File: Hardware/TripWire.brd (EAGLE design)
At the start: 37.2 x 50.3 mm, 67 parts, among them P1 LSP11, P2 LSP11, P3 LSP11, P4 LSP11, P5 LSP11, P6 LSP11, P7 LSP11, X1 GADGETEER-SOCKET

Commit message: Moved OSHW logo.
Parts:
- moved LOGO1 28.1 mm to (15.6, 32.3)
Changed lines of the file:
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@@
 <layer number="151" name="HeatSink" color="14" fill="1" visible="no" active="no"/>
 <layer number="199" name="Contour" color="7" fill="1" visible="no" active="no"/>
-<layer number="200" name="200bmp" color="7" fill="10" visible="yes" active="yes"/>
-<layer number="201" name="201bmp" color="15" fill="10" visible="yes" active="yes"/>
+<layer number="200" name="200bmp" color="7" fill="10" visible="no" active="yes"/>
+<layer number="201" name="201bmp" color="15" fill="10" visible="no" active="yes"/>
 <layer number="202" name="202bmp" color="7" fill="1" visible="no" active="yes"/>
 <layer number="203" name="203bmp" color="7" fill="1" visible="no" active="yes"/>
@@
 <circle x="33.6346" y="3.6016" radius="3.5355" width="0.4064" layer="20"/>
 <circle x="3.58" y="3.5" radius="3.5355" width="0.4064" layer="20"/>
-<text x="11.30401875" y="7.79131875" size="1.27" layer="21" ratio="12" rot="SR270">TripWire</text>
-<text x="9.830821875" y="5.330059375" size="0.8128" layer="21" ratio="12" rot="SR270">1.2</text>
+<text x="11.81201875" y="9.06131875" size="1.4224" layer="21" ratio="12" rot="SR270">TripWire</text>
+<text x="9.932421875" y="6.320659375" size="1.016" layer="21" ratio="12" rot="SR270">1.2</text>
 <text x="5.4102" y="41.7576" size="1.016" layer="21" ratio="12" rot="SR270">http://ianlee.info</text>
 <text x="-0.6096" y="-3.2512" size="1.778" layer="21">Corner holes are non-plated</text>
@@
 <wire x1="27.0002" y1="10.5918" x2="37.1094" y2="10.5918" width="0.4064" layer="21"/>
 <wire x1="37.1094" y1="10.5918" x2="37.1094" y2="39.8526" width="0.4064" layer="21"/>
-<wire x1="37.1856" y1="30.2768" x2="26.797" y2="30.2768" width="0.4064" layer="21"/>
+<wire x1="37.0586" y1="30.2768" x2="27.051" y2="30.2768" width="0.4064" layer="21"/>
 <wire x1="37.1856" y1="20.193" x2="27.1526" y2="20.193" width="0.4064" layer="21"/>
 <wire x1="20.6756" y1="0.0254" x2="23.41371875" y2="0.0254" width="0.4064" layer="21"/>
@@
 <attribute name="VALUE" x="2.295" y="17.7838" size="0.0254" layer="27" rot="R90"/>
 </element>
-<element name="LOGO1" library="SparkFun-Aesthetics" package="OSHW-LOGO-M" value="OSHW-LOGOM" x="27.0256" y="6.5278" rot="R270"/>
+<element name="LOGO1" library="SparkFun-Aesthetics" package="OSHW-LOGO-M" value="OSHW-LOGOM" x="15.6464" y="32.258" rot="R270"/>
 <element name="R22" library="SparkFun-Resistors" package="0603-RES" value="10" x="17.833340625" y="22.10561875" smashed="yes">
 <attribute name="NAME" x="19.382740625" y="21.80081875" size="0.6096" layer="25" font="vector"/>

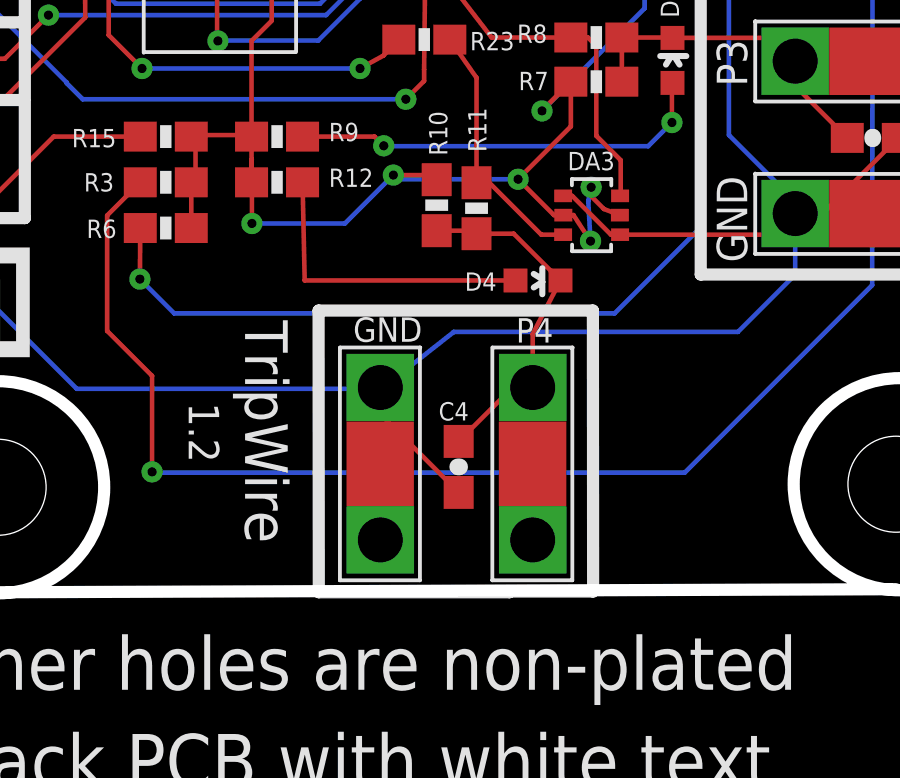
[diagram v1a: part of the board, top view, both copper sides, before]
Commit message: Adjusted font & silk around P4.
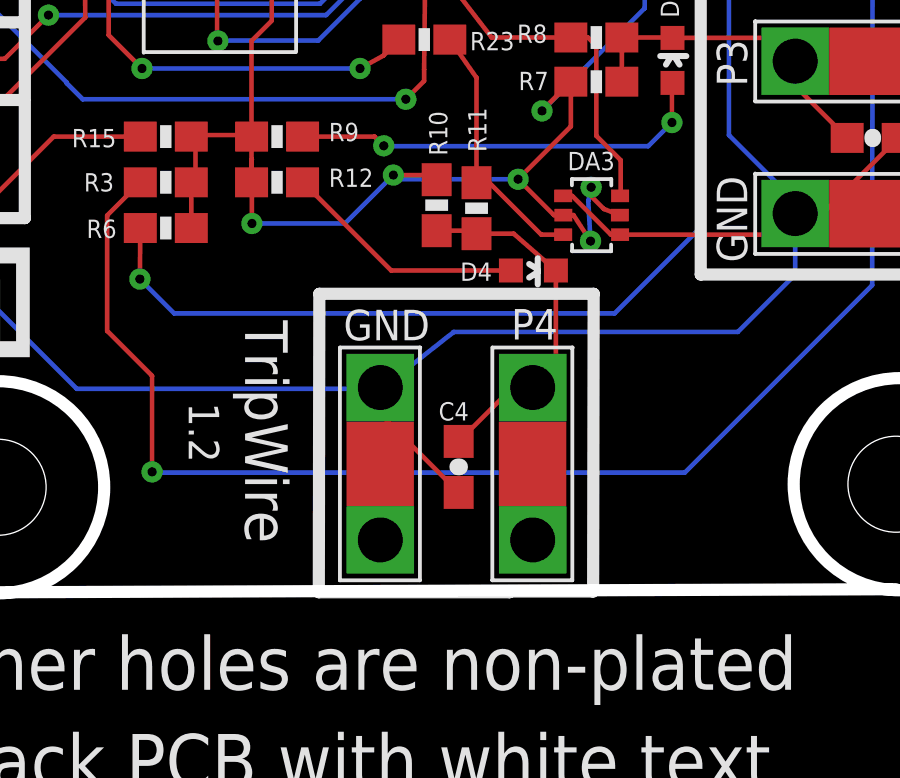
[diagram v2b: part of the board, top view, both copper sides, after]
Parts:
- moved D4 0.36 mm to (21.4, 10.7)
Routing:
- net N$7: track 10.3 -> 8.15 mm
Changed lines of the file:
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@@
 <text x="28.5242" y="27.051" size="1.016" layer="25" rot="R90">P2</text>
 <text x="28.5496" y="16.8656" size="1.016" layer="25" rot="R90">P3</text>
-<text x="22.0853" y="9.136378125" size="0.8128" layer="25" rot="R180">P4</text>
+<text x="22.2377" y="9.441178125" size="1.016" layer="25" rot="R180">P4</text>
 <text x="15.483840625" y="48.73498125" size="1.016" layer="25">P5</text>
 <text x="18.023840625" y="48.68418125" size="1.016" layer="25">P6</text>
@@
 <text x="28.5242" y="31.3436" size="1.016" layer="21" rot="R90">GND</text>
 <text x="28.5496" y="10.9982" size="1.016" layer="21" rot="R90">GND</text>
-<text x="17.7165" y="9.161778125" size="0.8128" layer="21" rot="R180">GND</text>
+<text x="17.9705" y="9.415778125" size="1.016" layer="21" rot="R180">GND</text>
 <text x="14.798040625" y="46.21658125" size="0.6096" layer="21" rot="R90">GND</text>
 <text x="6.1722" y="30.5816" size="1.4224" layer="21" rot="SR270">XY</text>
@@
 <wire x1="37.1856" y1="20.193" x2="27.1526" y2="20.193" width="0.4064" layer="21"/>
 <wire x1="20.6756" y1="0.0254" x2="23.41371875" y2="0.0254" width="0.4064" layer="21"/>
-<wire x1="23.41371875" y1="0.0254" x2="23.4061" y2="9.390378125" width="0.4064" layer="21"/>
-<wire x1="23.4061" y1="9.390378125" x2="14.2621" y2="9.390378125" width="0.4064" layer="21"/>
-<wire x1="14.2621" y1="9.390378125" x2="14.26971875" y2="0" width="0.4064" layer="21"/>
+<wire x1="23.41371875" y1="0.0254" x2="23.4315" y2="9.949178125" width="0.4064" layer="21"/>
+<wire x1="23.4315" y1="9.949178125" x2="14.2875" y2="9.949178125" width="0.4064" layer="21"/>
+<wire x1="14.2875" y1="9.949178125" x2="14.26971875" y2="0" width="0.4064" layer="21"/>
 <wire x1="14.26971875" y1="0" x2="20.6248" y2="0" width="0.4064" layer="21"/>
 <wire x1="20.6248" y1="0" x2="20.6248" y2="0.0254" width="0.4064" layer="21"/>
@@
 <attribute name="VALUE" x="11.7094" y="15.0114" size="0.4064" layer="27" font="vector"/>
 </element>
-<element name="D4" library="SparkFun-LED" package="LED-0603" value="Green 10mA" x="21.574759375" y="10.393678125" smashed="yes" rot="R270">
-<attribute name="PROD_ID" value="DIO-09003" x="44.434759375" y="23.093678125" size="1.778" layer="27" rot="R270" display="off"/>
-<attribute name="NAME" x="19.136359375" y="10.050778125" size="0.6096" layer="25"/>
+<element name="D4" library="SparkFun-LED" package="LED-0603" value="Green 10mA" x="21.422359375" y="10.723878125" smashed="yes" rot="R270">
+<attribute name="PROD_ID" value="DIO-09003" x="44.282359375" y="23.423878125" size="1.778" layer="27" rot="R270" display="off"/>
+<attribute name="NAME" x="18.983959375" y="10.380978125" size="0.6096" layer="25"/>
 </element>
 <element name="R10" library="SparkFun-Resistors" package="0603-RES" value="100K" x="18.1991" y="12.9032" smashed="yes" rot="R270">
@@
 <contactref element="U$7" pad="P$1"/>
 <contactref element="C4" pad="1"/>
-<wire x1="22.324759375" y1="10.393678125" x2="21.3995" y2="8.608759375" width="0.154" layer="1"/>
-<wire x1="21.3995" y1="8.608759375" x2="21.3995" y2="6.824978125" width="0.154" layer="1"/>
 <wire x1="19.527521875" y1="11.9516" x2="19.425921875" y2="12.0532" width="0.154" layer="1"/>
 <wire x1="19.425921875" y1="12.0532" x2="18.1991" y2="12.0532" width="0.154" layer="1"/>
-<wire x1="22.324759375" y1="10.393678125" x2="20.7668375" y2="11.9516" width="0.154" layer="1"/>
+<wire x1="22.172359375" y1="10.723878125" x2="20.7668375" y2="11.9516" width="0.154" layer="1"/>
 <wire x1="20.7668375" y1="11.9516" x2="19.527521875" y2="11.9516" width="0.154" layer="1"/>
 <wire x1="18.93188125" y1="5.029540625" x2="20.709540625" y2="6.8072" width="0.154" layer="1"/>
 <wire x1="20.709540625" y1="6.8072" x2="21.4122" y2="6.8072" width="0.154" layer="1"/>
+<wire x1="21.4122" y1="6.8072" x2="21.3995" y2="6.824978125" width="0" layer="19" extent="1-1"/>
+<wire x1="22.172359375" y1="10.723878125" x2="22.172359375" y2="7.567359375" width="0.154" layer="1"/>
+<wire x1="22.172359375" y1="7.567359375" x2="21.4122" y2="6.8072" width="0.154" layer="1"/>
 <wire x1="21.4122" y1="6.8072" x2="21.3995" y2="6.824978125" width="0" layer="19" extent="1-16"/>
 </signal>
@@
 <contactref element="R12" pad="2"/>
 <contactref element="D4" pad="A"/>
-<wire x1="13.7278" y1="13.6652" x2="13.798921875" y2="10.393678125" width="0.154" layer="1"/>
-<wire x1="13.798921875" y1="10.393678125" x2="20.824759375" y2="10.393678125" width="0.154" layer="1"/>
+<wire x1="20.672359375" y1="10.723878125" x2="16.682721875" y2="10.723878125" width="0.154" layer="1"/>
+<wire x1="16.682721875" y1="10.723878125" x2="13.7414" y2="13.6652" width="0.154" layer="1"/>
+<wire x1="13.7414" y1="13.6652" x2="13.7278" y2="13.6652" width="0" layer="19" extent="1-16"/>
 </signal>
 <signal name="N$14">

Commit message: Fixed bad connection on D6.
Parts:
- moved R15 23.5 mm to (16.1, 37.7), turned to 90 degrees
- moved R6 1.45 mm to (9.25, 13.6)
- moved R3 1.45 mm to (9.25, 15.1)
- moved LOGO1 0.96 mm to (16.4, 32.9)
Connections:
- removed net N$23: C6.1, R16.2, R17.2
- net N$9: now also C6.1, R16.2, R17.2
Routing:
- net N$13: track 51.9 -> 4.09 mm, vias 2 -> 0
- net N$9: track 2.63 -> 25.6 mm, vias 0 -> 2
- net N$23: track 20.6 -> 0.00 mm, vias 2 -> 0
- net N$12: track 10.3 -> 4.51 mm, vias 2 -> 0
- net N$14: track 27.2 -> 23.1 mm
- net N$1: track 69.9 -> 71.7 mm
- net N$3: track 37.2 -> 38.4 mm
- net N$10: track 5.63 -> 5.52 mm, vias 2 -> 0

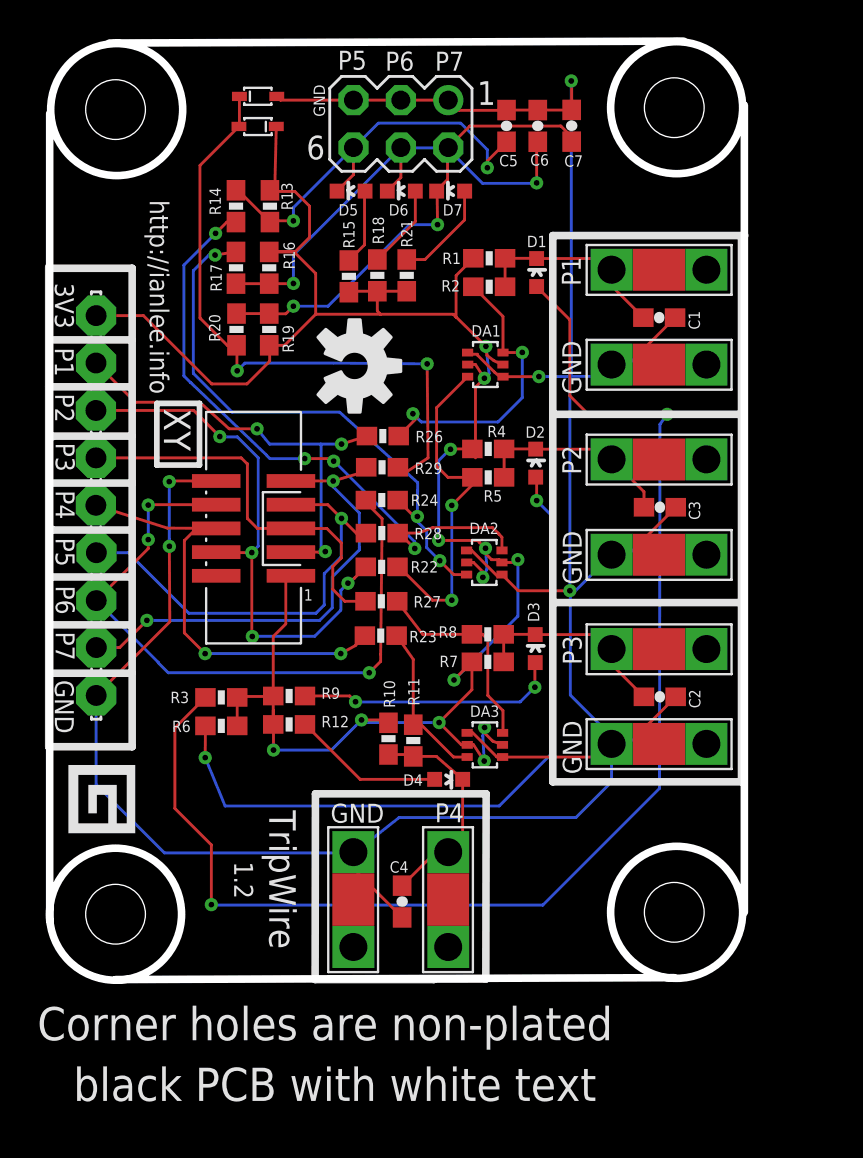
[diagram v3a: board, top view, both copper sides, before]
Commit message: Optimized some routes.
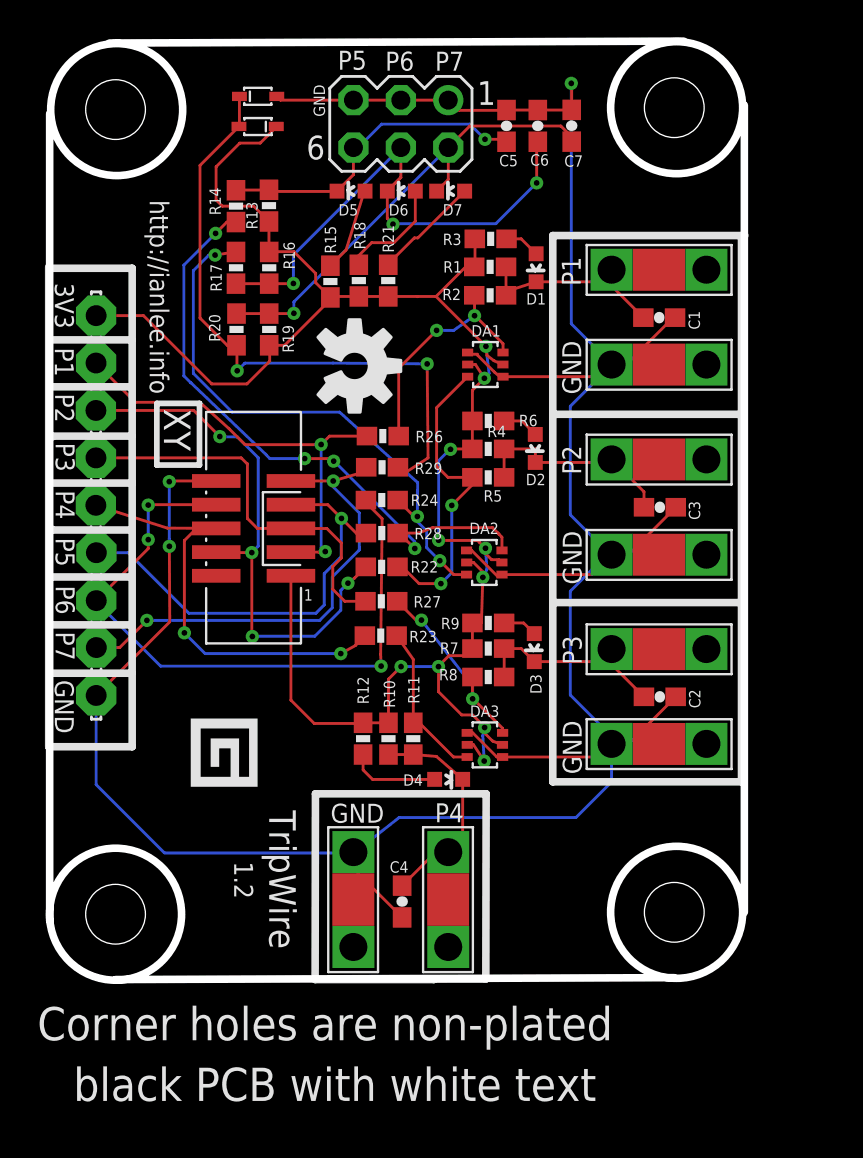
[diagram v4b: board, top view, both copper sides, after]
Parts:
- moved R3 28.5 mm to (23.7, 39.7), turned to 0 degrees
- moved R6 21.7 mm to (23.5, 29.9), turned to 180 degrees
- moved R9 11.4 mm to (23.5, 19.1)
- moved R12 4.04 mm to (16.8, 12.9), turned to 270 degrees
- moved R8 2.29 mm to (23.5, 16.2)
- moved R18 1.03 mm to (16.6, 37.4)
- moved R21 1.03 mm to (18.2, 37.4)
- moved R15 1.03 mm to (15.1, 37.4)
- moved D2 0.79 mm to (26.1, 28.4), turned to 180 degrees
- moved R7 0.71 mm to (23.5, 17.7)
- moved R1 0.46 mm to (23.6, 38.2)
- moved R2 0.46 mm to (23.6, 36.7)
- moved D1 0.26 mm to (26.1, 38.1), turned to 180 degrees
- moved R11 0.10 mm to (19.5, 12.9)
- moved D3 0.07 mm to (26.0, 17.8), turned to 180 degrees
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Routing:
- net N$1: track 71.7 -> 1.92 mm, vias 2 -> 0
- net N$3: track 38.4 -> 2.00 mm, vias 2 -> 0
- net 3V3: track 117.5 -> 101.6 mm, vias 13 -> 10
- net N$5: track 14.1 -> 1.84 mm, vias 2 -> 0
- net N$14: track 23.1 -> 17.3 mm, vias 2 -> 1
- net GND: track 151.8 -> 155.7 mm, vias 5 -> 3
- net PIN3: track 16.0 -> 12.5 mm
- net N$9: track 25.6 -> 29.1 mm, vias 2 -> 3
- net N$7: track 8.15 -> 4.87 mm
- net PIN4: track 18.7 -> 16.8 mm
- net N$12: track 4.51 -> 5.90 mm
- net N$6: track 24.7 -> 25.5 mm, vias 2 -> 1
- net PIN5: track 11.2 -> 10.5 mm, vias 0 -> 2
- net N$2: track 10.8 -> 11.4 mm
- net N$18: track 24.1 -> 24.3 mm, vias 3 -> 2

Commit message: Eliminated some vias.
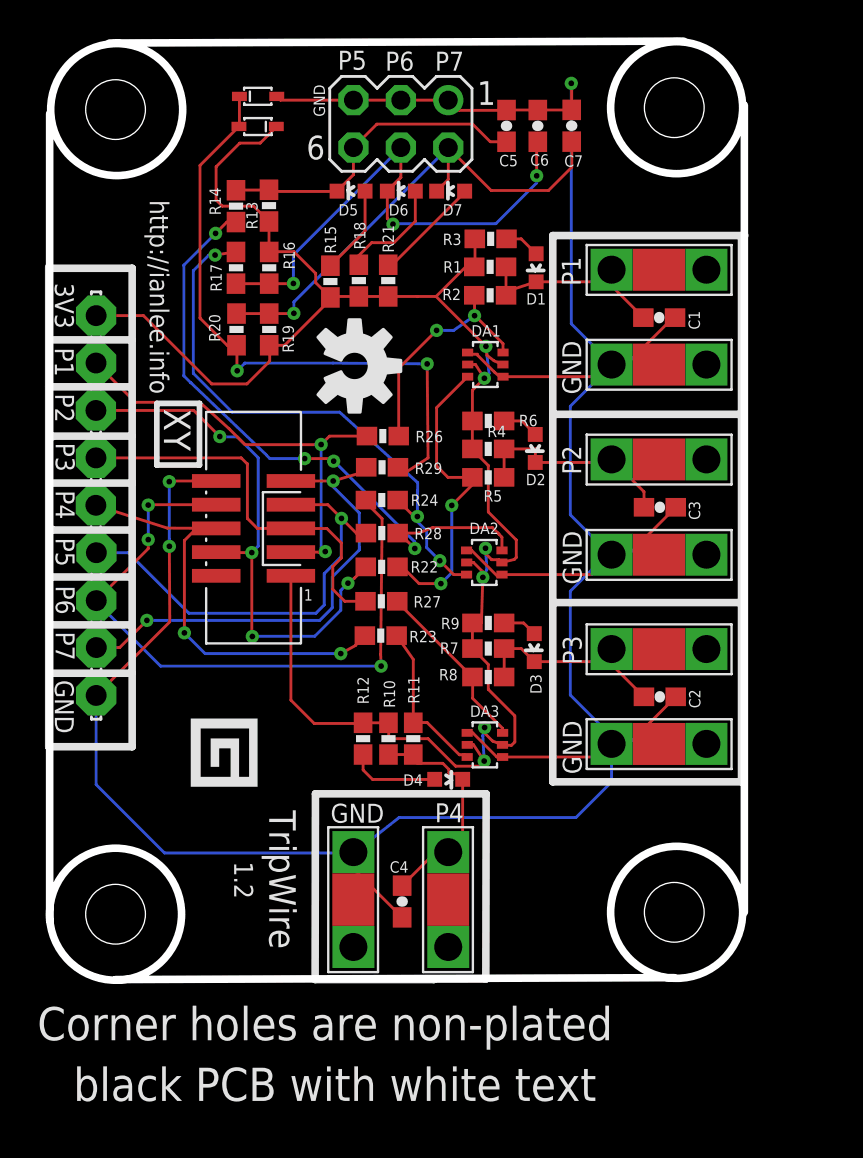
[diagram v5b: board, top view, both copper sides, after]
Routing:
- net N$6: track 25.5 -> 27.6 mm
- net PIN5: track 10.5 -> 9.41 mm, vias 2 -> 0
- net 3V3: track 101.6 -> 101.3 mm, vias 10 -> 6
- net N$14: vias 1 -> 0

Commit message: Added ground planes.
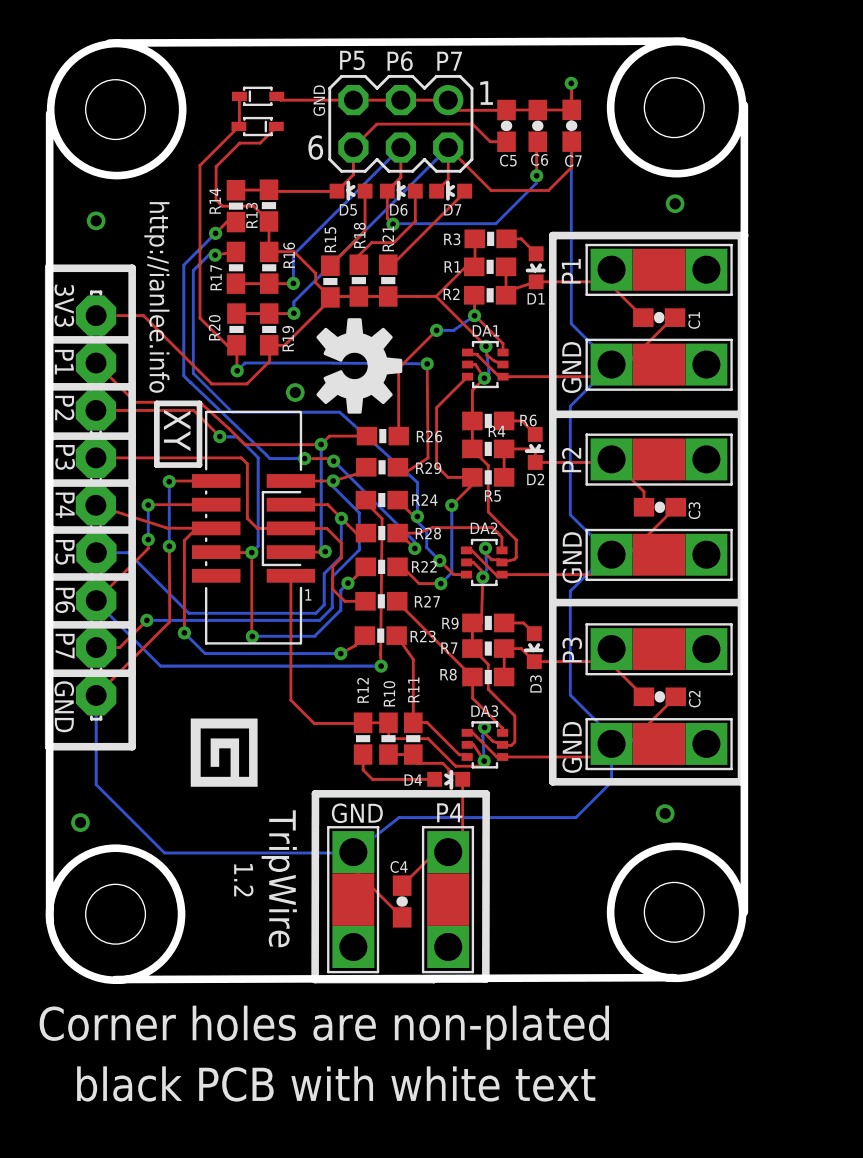
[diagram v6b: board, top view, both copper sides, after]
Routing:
- net GND: vias 3 -> 8
- added copper zone on layer 1, net GND
- added copper zone on layer 16, net GND
